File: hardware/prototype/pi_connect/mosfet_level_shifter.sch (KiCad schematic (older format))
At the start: 3 parts, among them Q1 2N7000

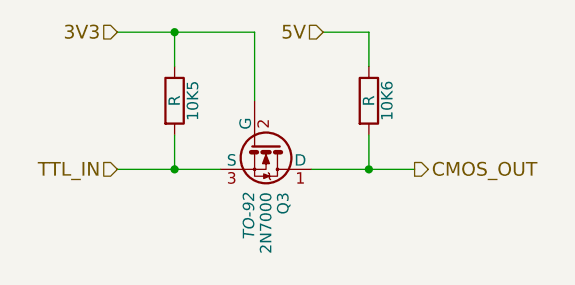
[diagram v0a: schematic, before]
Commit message: Assign footprints
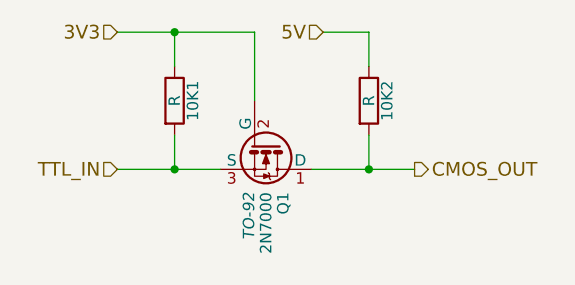
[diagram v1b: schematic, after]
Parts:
- 10K1, 10K2: footprint (none) -> Resistors_ThroughHole:Resistor_Horizontal_RM10mm
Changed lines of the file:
@@
 AR Path="/5798D753/5798C5FD" Ref="10K3"  Part="1"
 AR Path="/5798D9BB/5798C5FD" Ref="10K5"  Part="1"
-F 0 "10K5" V 1230 1000 50  0000 C CNN
+F 0 "10K1" V 1230 1000 50  0000 C CNN
 F 1 "R" V 1150 1000 50  0000 C CNN
-F 2 "" V 1080 1000 50  0000 C CNN
+F 2 "Resistors_ThroughHole:Resistor_Horizontal_RM10mm" V 1080 1000 50  0001 C CNN
 F 3 "" H 1150 1000 50  0000 C CNN
 	1    1150 1000
@@
 AR Path="/5798D753/5798C628" Ref="10K4"  Part="1"
 AR Path="/5798D9BB/5798C628" Ref="10K6"  Part="1"
-F 0 "10K6" V 2080 1000 50  0000 C CNN
+F 0 "10K2" V 2080 1000 50  0000 C CNN
 F 1 "R" V 2000 1000 50  0000 C CNN
-F 2 "" V 1930 1000 50  0000 C CNN
+F 2 "Resistors_ThroughHole:Resistor_Horizontal_RM10mm" V 1930 1000 50  0001 C CNN
 F 3 "" H 2000 1000 50  0000 C CNN
 	1    2000 1000
@@
 AR Path="/5798D753/5798C66E" Ref="Q2"  Part="1"
 AR Path="/5798D9BB/5798C66E" Ref="Q3"  Part="1"
-F 0 "Q3" H 1750 1275 50  0000 L CNN
+F 0 "Q1" H 1750 1275 50  0000 L CNN
 F 1 "2N7000" H 1750 1200 50  0000 L CNN
 F 2 "TO-92" H 1750 1125 50  0000 L CIN

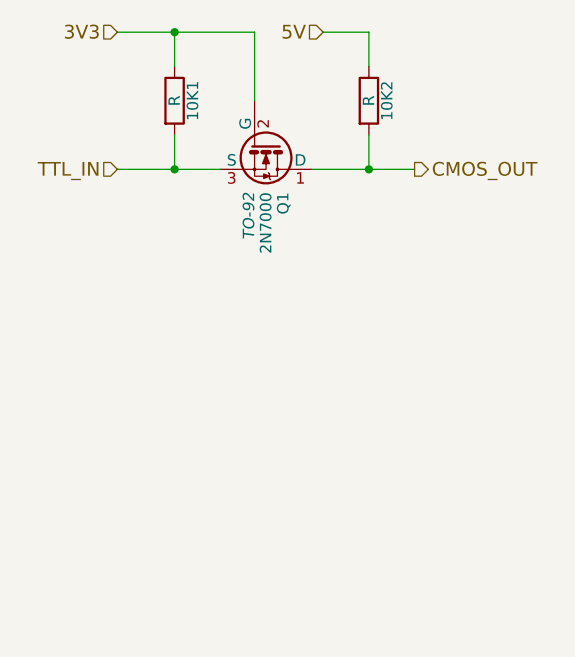
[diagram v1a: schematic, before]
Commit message: Add footprint fot SPDT switches according to datasheet for 100SP4T1B1M2QEH. Also attempted to route some of this complex circuit manually.
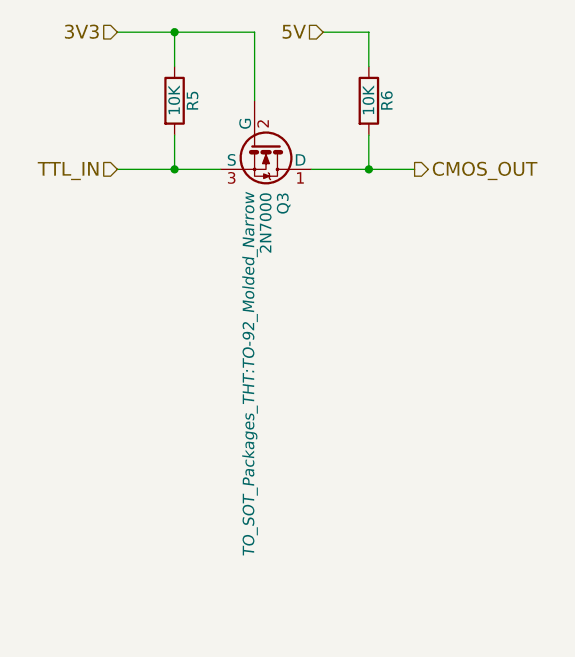
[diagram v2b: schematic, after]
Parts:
- Q1: footprint TO-92 -> TO_SOT_Packages_THT:TO-92_Molded_Narrow
- R3: renamed from 10K1; value R -> 10K
- R4: renamed from 10K2; value R -> 10K
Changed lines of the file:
@@
 LIBS:Pi2_Connector
 LIBS:MCP23017
+LIBS:prototype_pi_connect-cache
 EELAYER 25 0
 EELAYER END
 $Descr A4 11693 8268
 encoding utf-8
-Sheet 2 4
+Sheet 3 4
 Title ""
 Date ""
@@
 $EndDescr
 $Comp
-L R 10K1
+L R R3
 U 1 1 5798C5FD
 P 1150 1000
-AR Path="/5798C58F/5798C5FD" Ref="10K1"  Part="1"
-AR Path="/5798D753/5798C5FD" Ref="10K3"  Part="1"
-AR Path="/5798D9BB/5798C5FD" Ref="10K5"  Part="1"
-F 0 "10K1" V 1230 1000 50  0000 C CNN
-F 1 "R" V 1150 1000 50  0000 C CNN
+AR Path="/5798C58F/5798C5FD" Ref="R3"  Part="1"
+AR Path="/5798D753/5798C5FD" Ref="R7"  Part="1"
+AR Path="/5798D9BB/5798C5FD" Ref="R5"  Part="1"
+F 0 "R5" V 1230 1000 50  0000 C CNN
+F 1 "10K" V 1150 1000 50  0000 C CNN
 F 2 "Resistors_ThroughHole:Resistor_Horizontal_RM10mm" V 1080 1000 50  0001 C CNN
 F 3 "" H 1150 1000 50  0000 C CNN
@@
 $EndComp
 $Comp
-L R 10K2
+L R R4
 U 1 1 5798C628
 P 2000 1000
-AR Path="/5798C58F/5798C628" Ref="10K2"  Part="1"
-AR Path="/5798D753/5798C628" Ref="10K4"  Part="1"
-AR Path="/5798D9BB/5798C628" Ref="10K6"  Part="1"
-F 0 "10K2" V 2080 1000 50  0000 C CNN
-F 1 "R" V 2000 1000 50  0000 C CNN
+AR Path="/5798C58F/5798C628" Ref="R4"  Part="1"
+AR Path="/5798D753/5798C628" Ref="R8"  Part="1"
+AR Path="/5798D9BB/5798C628" Ref="R6"  Part="1"
+F 0 "R6" V 2080 1000 50  0000 C CNN
+F 1 "10K" V 2000 1000 50  0000 C CNN
 F 2 "Resistors_ThroughHole:Resistor_Horizontal_RM10mm" V 1930 1000 50  0001 C CNN
 F 3 "" H 2000 1000 50  0000 C CNN
@@
 AR Path="/5798D753/5798C66E" Ref="Q2"  Part="1"
 AR Path="/5798D9BB/5798C66E" Ref="Q3"  Part="1"
-F 0 "Q1" H 1750 1275 50  0000 L CNN
+F 0 "Q3" H 1750 1275 50  0000 L CNN
 F 1 "2N7000" H 1750 1200 50  0000 L CNN
-F 2 "TO-92" H 1750 1125 50  0000 L CIN
+F 2 "TO_SOT_Packages_THT:TO-92_Molded_Narrow" H 1750 1125 50  0000 L CIN
 F 3 "" H 1550 1200 50  0000 L CNN
 	1    1550 1200
